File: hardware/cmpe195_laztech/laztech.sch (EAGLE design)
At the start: 6 parts

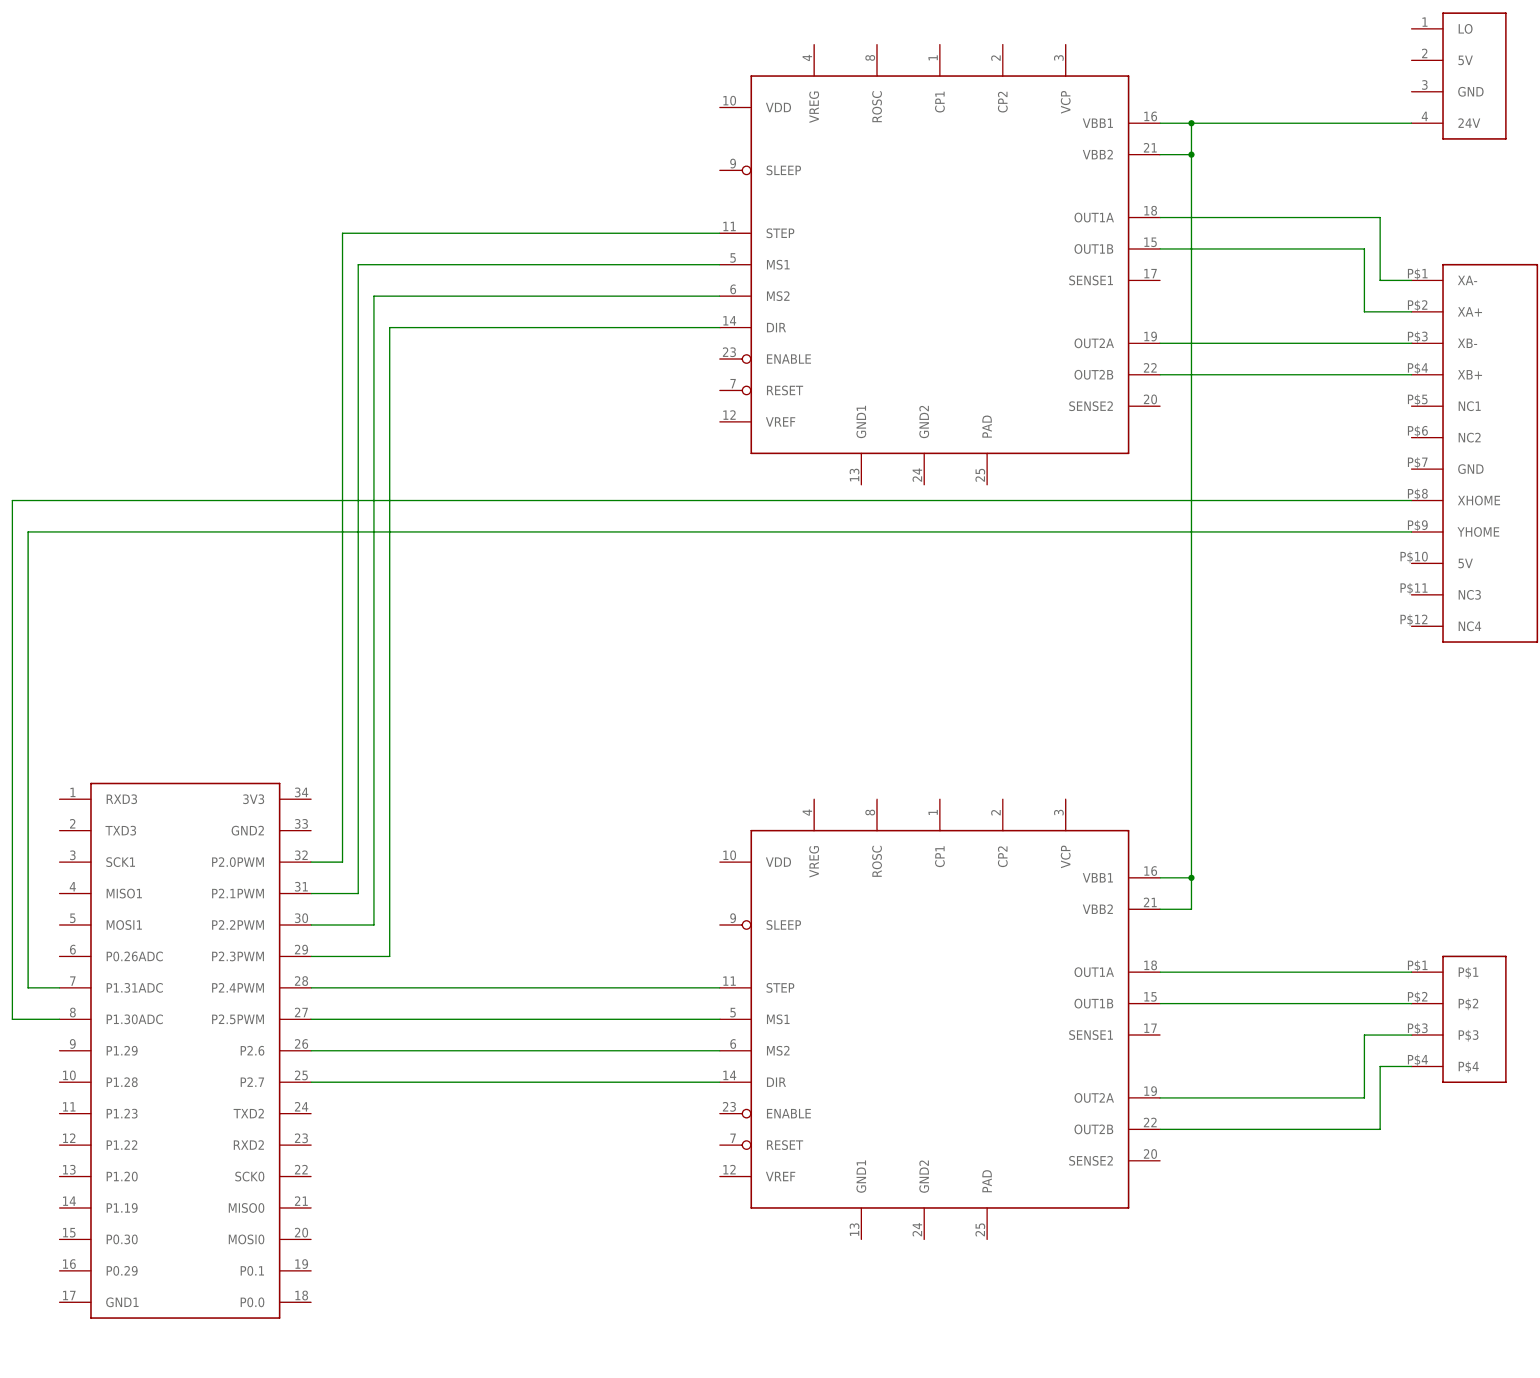
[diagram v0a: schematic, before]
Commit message: Added initial direct connections with no passives.
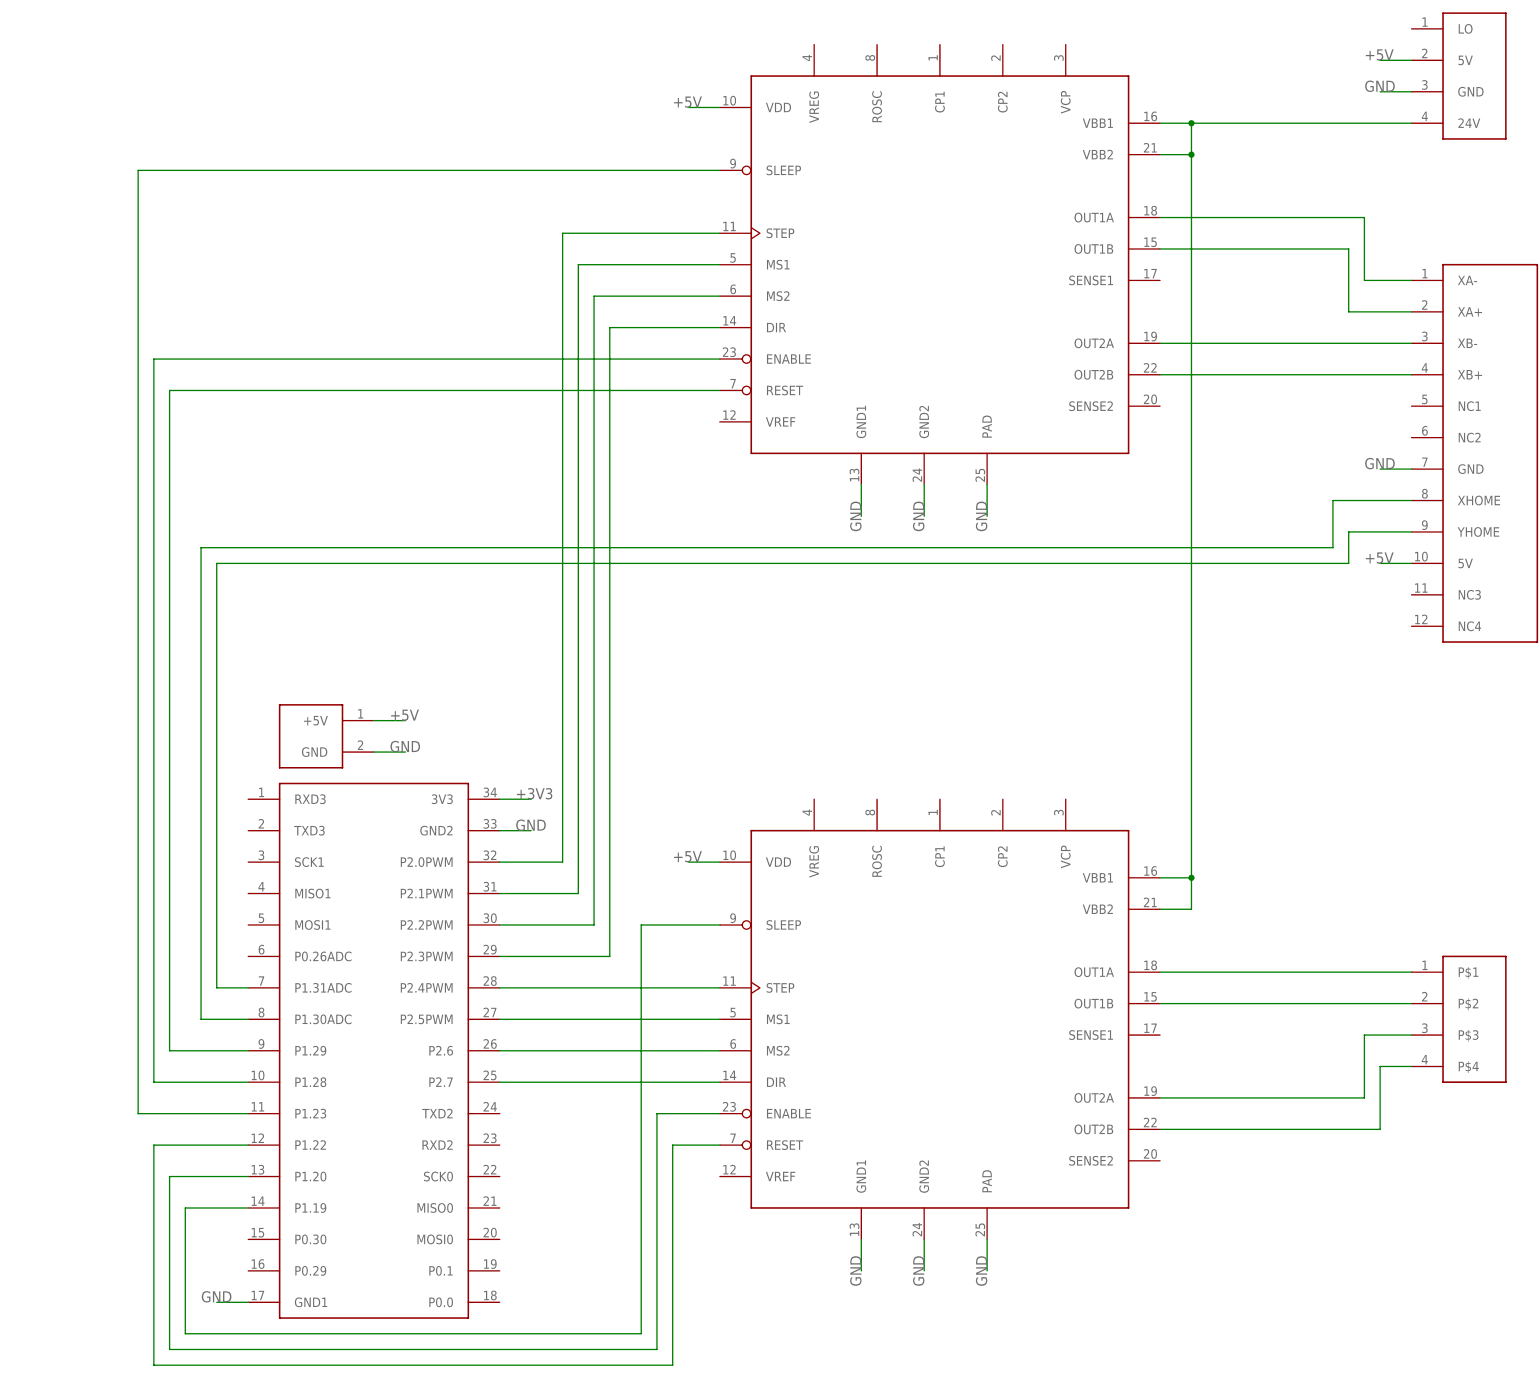
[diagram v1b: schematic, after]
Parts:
- added U$7: SJSUONEVIN, laztech_parts:SJSUONEVIN
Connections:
- new net +3V3: U$3.3V3
- new net +5V: U$1.VDD, U$2.VDD, U$4.5V, U$5.5V, U$7.+5V
- new net GND: U$1.GND1, U$1.GND2, U$1.PAD, U$2.GND1, U$2.GND2, U$2.PAD, U$3.GND1, U$3.GND2, U$4.GND, U$5.GND, U$7.GND
- new net N$20: U$2.ENABLE, U$3.P1.20
- new net N$21: U$2.RESET, U$3.P1.22
- new net N$22: U$2.SLEEP, U$3.P1.19
- new net N$23: U$1.RESET, U$3.P1.29
- new net N$24: U$1.ENABLE, U$3.P1.28
- new net N$25: U$1.SLEEP, U$3.P1.23

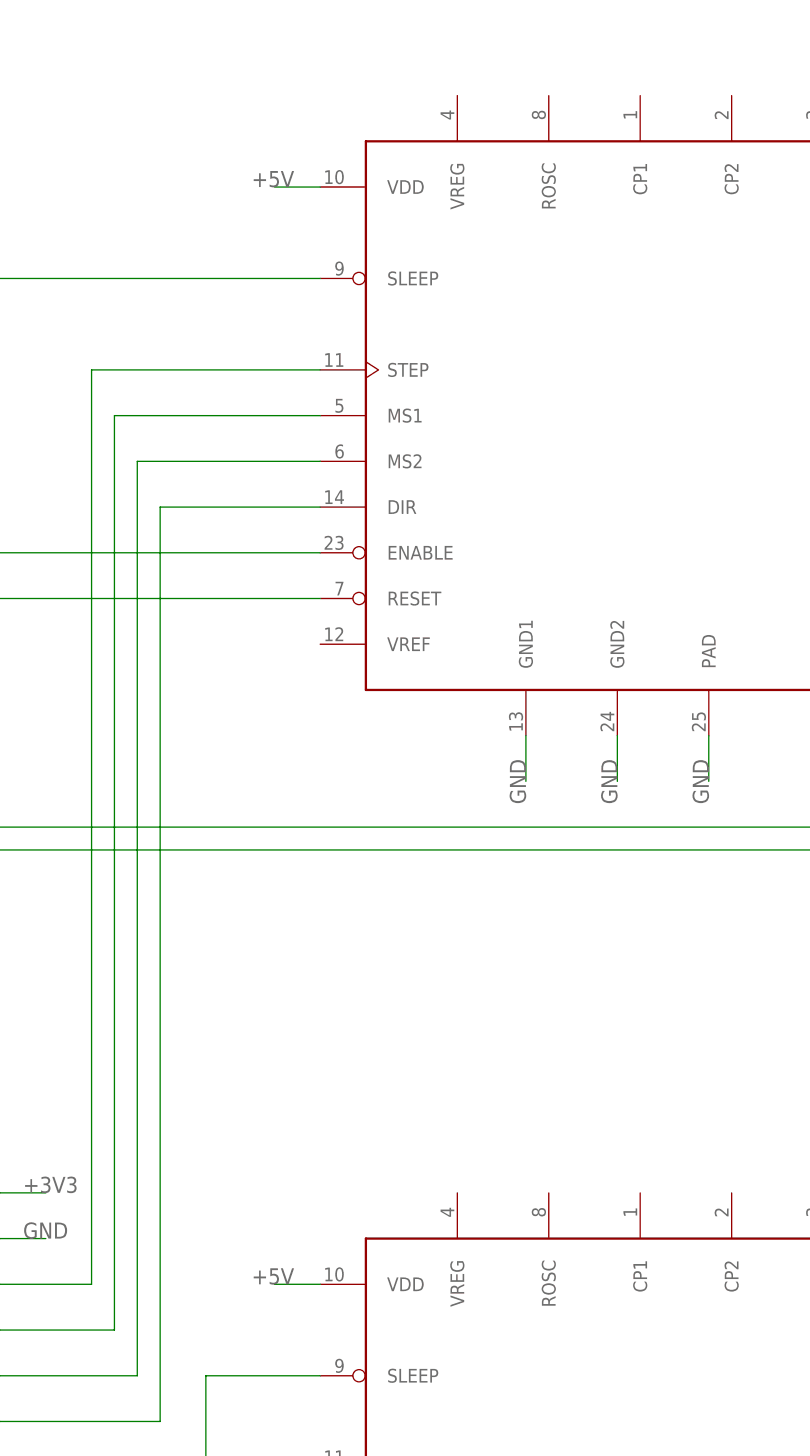
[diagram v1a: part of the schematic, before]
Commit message: Started board layout and added Rosc to ground.
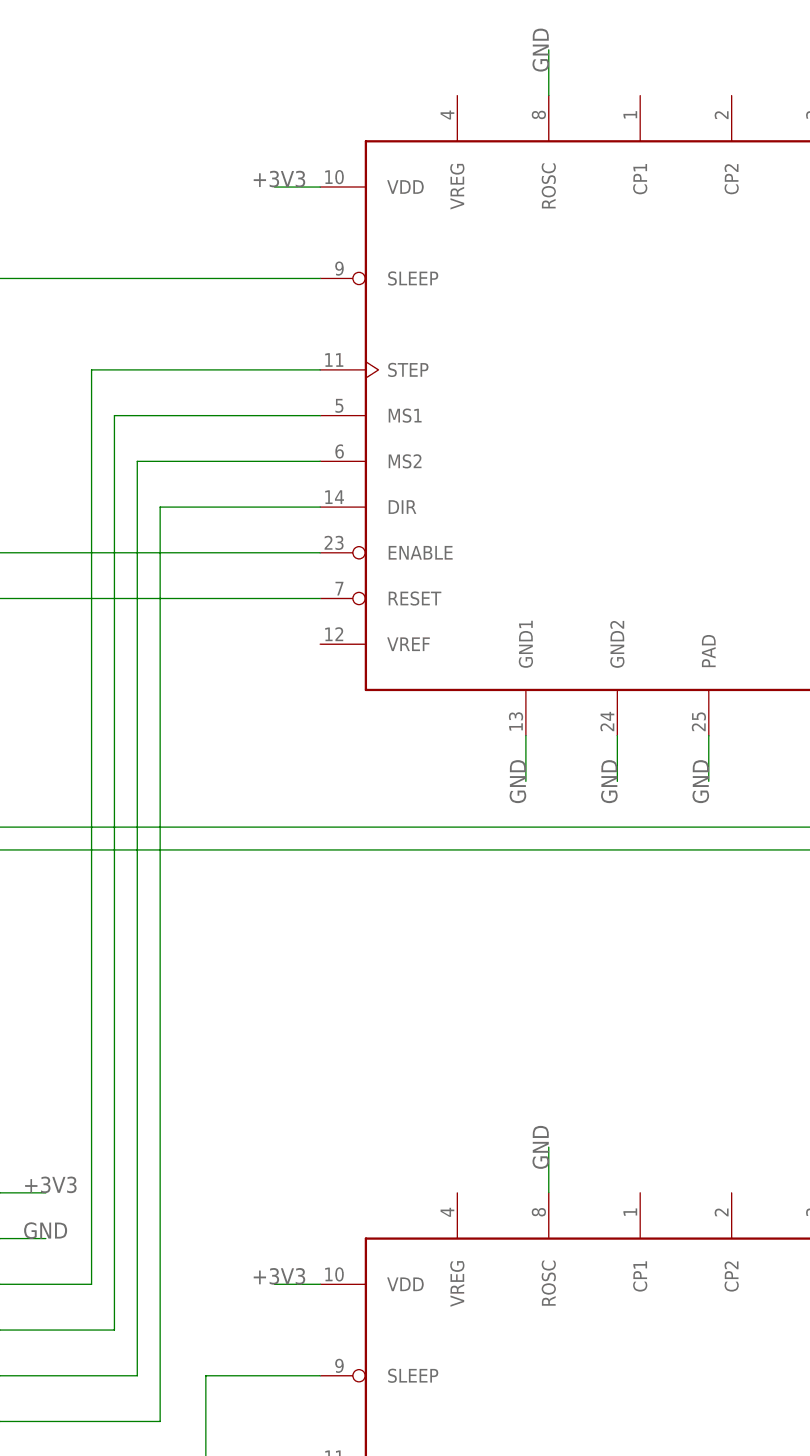
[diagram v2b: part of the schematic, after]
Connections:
- net +3V3: now also U$1.VDD, U$2.VDD
- net +5V: no longer U$1.VDD, U$2.VDD
- net GND: now also U$1.ROSC, U$2.ROSC
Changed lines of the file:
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@@
 <label x="231.14" y="149.86" size="1.778" layer="95"/>
+</segment>
+<segment>
+<pinref part="U$2" gate="G$1" pin="ROSC"/>
+<wire x1="309.88" y1="142.24" x2="309.88" y2="147.32" width="0.1524" layer="91"/>
+<label x="309.88" y="144.78" size="1.778" layer="95" rot="R90"/>
+</segment>
+<segment>
+<pinref part="U$1" gate="G$1" pin="ROSC"/>
+<wire x1="309.88" y1="264.16" x2="309.88" y2="269.24" width="0.1524" layer="91"/>
+<label x="309.88" y="266.7" size="1.778" layer="95" rot="R90"/>
 </segment>
 </net>
@@
 <label x="251.46" y="142.24" size="1.778" layer="95"/>
 </segment>
-</net>
-<net name="+5V" class="0">
 <segment>
 <pinref part="U$2" gate="G$1" pin="VDD"/>
@@
 <label x="276.86" y="254" size="1.778" layer="95"/>
 </segment>
+</net>
+<net name="+5V" class="0">
 <segment>
 <pinref part="U$4" gate="G$1" pin="5V"/>

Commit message: Replaced some connectors with SFE connecters.
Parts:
- U$3: value SJSUONE -> SJSUONEX; device laztech_parts:SJSUONE -> laztech_parts:SJSUONEX
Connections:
- net +5V: now also U$5.+5V; no longer U$5.5V
- net N$1: now also U$5.XB+; no longer U$5.XA-
- net N$10: now also U$5.XHOME; no longer U$5.YHOME
- net N$11: now also U$5.YHOME; no longer U$5.XHOME
- net N$2: now also U$5.XB-; no longer U$5.XA+
- net N$3: now also U$5.XA+; no longer U$5.XB-
- net N$4: now also U$5.XA-; no longer U$5.XB+
- net N$5: now also U$6.YA-; no longer U$6.P$1
- net N$6: now also U$6.YA+; no longer U$6.P$2
- net N$7: now also U$6.YB-; no longer U$6.P$3
- net N$8: now also U$6.YB+; no longer U$6.P$4

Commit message: Fixed more parts in library.
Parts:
- U$4: value K40KK -> K40-PWR; device laztech_parts:K40KK -> laztech_parts:K40-PWR
- U$5: value K40FFC -> K40-X; device laztech_parts:K40FFC -> laztech_parts:K40-X
- U$6: value K40JST -> K40-Y; device laztech_parts:K40JST -> laztech_parts:K40-Y
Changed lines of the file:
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@@
 <part name="U$2" library="laztech_parts" deviceset="A4985SLPTR-T" device=""/>
 <part name="U$3" library="laztech_parts" deviceset="SJSUONEX" device=""/>
-<part name="U$4" library="laztech_parts" deviceset="K40KK" device=""/>
-<part name="U$5" library="laztech_parts" deviceset="K40FFC" device=""/>
-<part name="U$6" library="laztech_parts" deviceset="K40JST" device=""/>
+<part name="U$4" library="laztech_parts" deviceset="K40-PWR" device=""/>
+<part name="U$5" library="laztech_parts" deviceset="K40-X" device=""/>
+<part name="U$6" library="laztech_parts" deviceset="K40-Y" device=""/>
 <part name="U$7" library="laztech_parts" deviceset="SJSUONEVIN" device=""/>
 </parts>
